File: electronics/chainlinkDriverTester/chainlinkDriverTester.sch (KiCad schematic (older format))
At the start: 144 parts, among them J1 Barrel_Jack_Switch, J10 Sensor C, J11 Sensor D, J12 Motor E, J13 Motor F, J14 Sensor E, J15 Sensor F, J2 Conn_01x03_Female, J22 Power, J26 exp, J27 exp, J28 exp, J29 exp, J3 Motor A, J30 exp, J31 exp, J32 Conn_01x06_Female, J5 Motor B, J6 Motor C, J7 Motor D, J8 Sensor A, J9 Sensor B, SW1 SW_Push, U1 AP7361C-33E, U2 TTGO_TDisplay, U3 VN7007ALH, U4 MCP23017_SS, U5 INA219BxD, U7 Buck

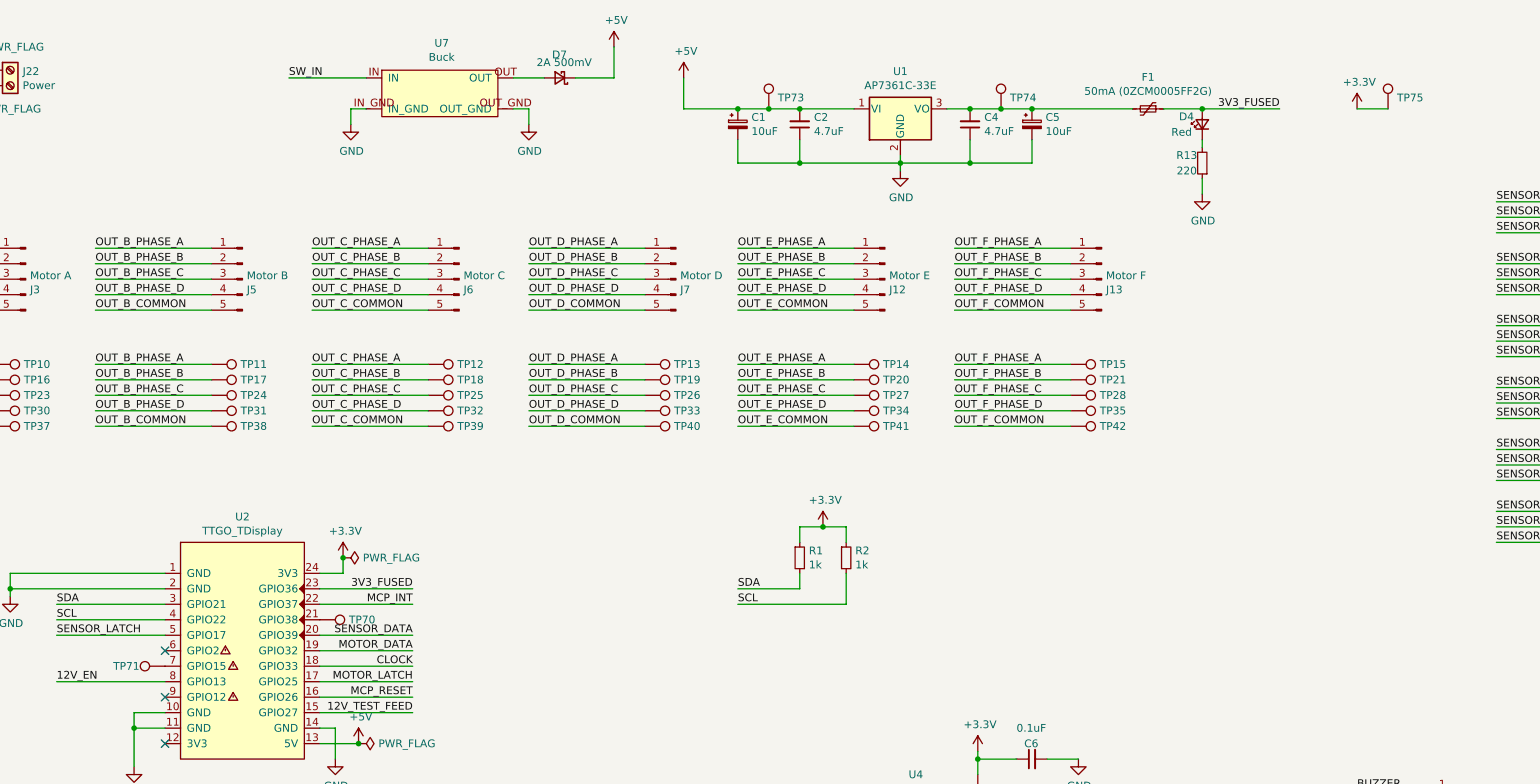
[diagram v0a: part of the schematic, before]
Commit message: Update chainlink driver tester PCB to match schematic with updated T-Display pinout, add extra row of holes for each pin for convenience
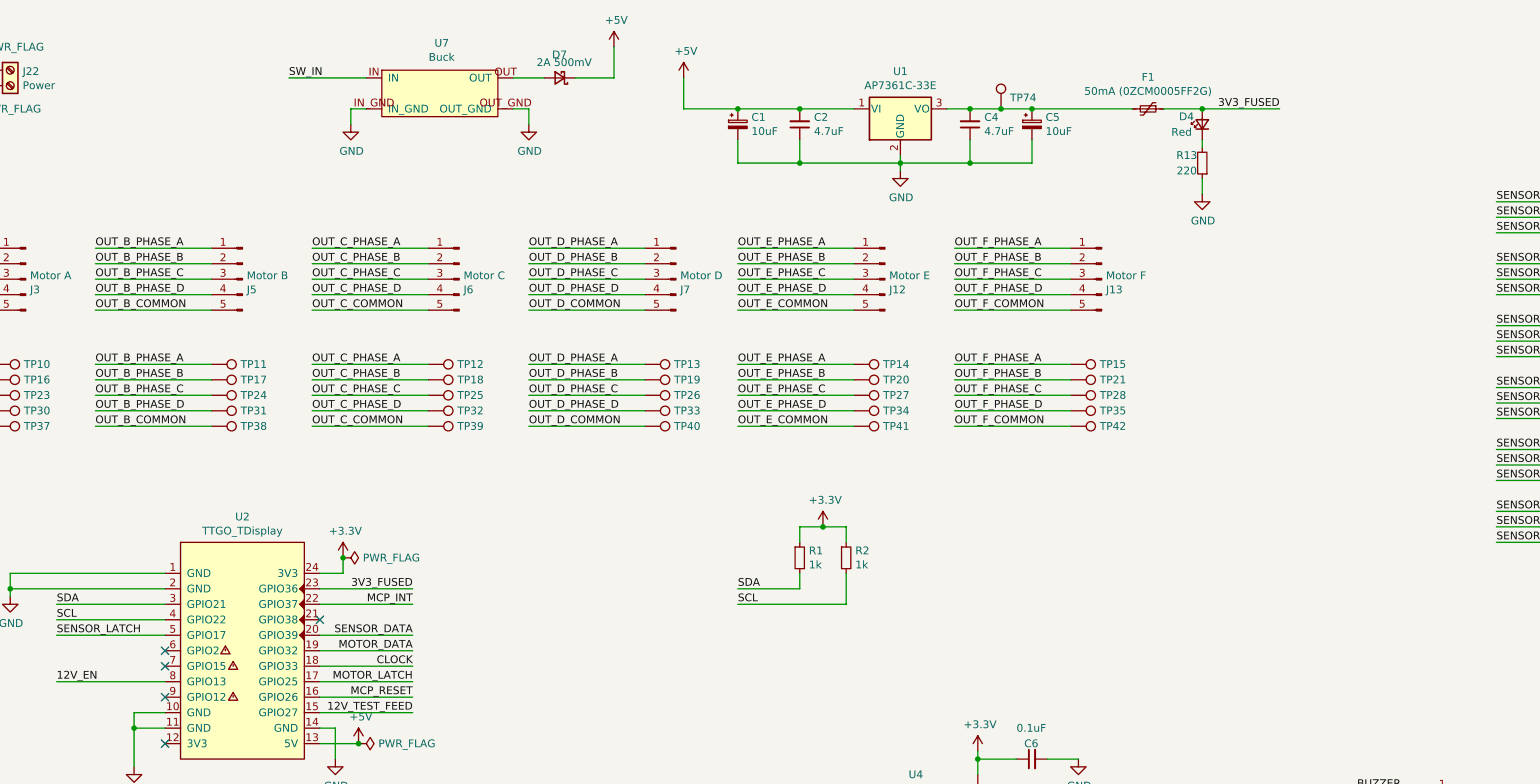
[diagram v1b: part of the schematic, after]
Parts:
- removed TP70, TP71, TP73, TP75: TestPoint, TestPoint:TestPoint_THTPad_D2.0mm_Drill1.0mm, symbol Connector:TestPoint
- U2: footprint ESP32:T-DISPLAY -> ESP32:T-DISPLAY_extra_pins
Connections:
- no-connect marks 20 -> 22
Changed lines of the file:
@@
 F 0 "U2" H 3100 5465 50  0000 C CNN
 F 1 "TTGO_TDisplay" H 3100 5374 50  0000 C CNN
-F 2 "ESP32:T-DISPLAY" H 2900 4650 50  0001 C CNN
+F 2 "ESP32:T-DISPLAY_extra_pins" H 2900 4650 50  0001 C CNN
 F 3 "" H 2900 4650 50  0001 C CNN
 	1    3100 4600
@@
 Connection ~ 6300 1100
 Wire Wire Line
-	6300 1100 6500 1100
-Wire Wire Line
 	6300 1300 6300 1450
 Wire Wire Line
@@
 NoConn ~ 15700 1300
 NoConn ~ 15950 1300
-$Comp
-L Connector:TestPoint TP70
-U 1 1 62B87233
-P 3600 4400
-F 0 "TP70" V 3600 4588 50  0000 L CNN
-F 1 "TestPoint" V 3645 4588 50  0001 L CNN
-F 2 "TestPoint:TestPoint_THTPad_D2.0mm_Drill1.0mm" H 3800 4400 50  0001 C CNN
-F 3 "~" H 3800 4400 50  0001 C CNN
-	1    3600 4400
-	0    1    1    0
-$EndComp
 Wire Wire Line
 	8200 1100 8850 1100
@@
 Wire Wire Line
 	8000 1100 8200 1100
-$Comp
-L Connector:TestPoint TP73
-U 1 1 62BEB5EB
-P 6500 1100
-F 0 "TP73" H 6558 1172 50  0000 L CNN
-F 1 "TestPoint" V 6545 1288 50  0001 L CNN
-F 2 "TestPoint:TestPoint_THTPad_D2.0mm_Drill1.0mm" H 6700 1100 50  0001 C CNN
-F 3 "~" H 6700 1100 50  0001 C CNN
-	1    6500 1100
-	1    0    0    -1
-$EndComp
-Connection ~ 6500 1100
-Wire Wire Line
-	6500 1100 6700 1100
-$Comp
-L Connector:TestPoint TP75
-U 1 1 62BF431E
-P 10500 1100
-F 0 "TP75" H 10558 1172 50  0000 L CNN
-F 1 "TestPoint" V 10545 1288 50  0001 L CNN
-F 2 "TestPoint:TestPoint_THTPad_D2.0mm_Drill1.0mm" H 10700 1100 50  0001 C CNN
-F 3 "~" H 10700 1100 50  0001 C CNN
-	1    10500 1100
-	1    0    0    -1
-$EndComp
-$Comp
-L power:+3.3V #PWR01
-U 1 1 62BFECBC
-P 10300 1100
-F 0 "#PWR01" H 10300 950 50  0001 C CNN
-F 1 "+3.3V" H 10315 1273 50  0000 C CNN
-F 2 "" H 10300 1100 50  0001 C CNN
-F 3 "" H 10300 1100 50  0001 C CNN
-	1    10300 1100
-	1    0    0    -1
-$EndComp
-Wire Wire Line
-	10300 1100 10500 1100
 Text Label 14500 4300 0    50   ~ 0
 SW_IN
@@
 	1    9300 1650
 	1    0    0    -1
-$EndComp
-$Comp
-L Connector:TestPoint TP71
-U 1 1 62B8767D
-P 2600 4700
-F 0 "TP71" V 2600 4950 50  0000 C CNN
-F 1 "TestPoint" V 2704 4772 50  0001 C CNN
-F 2 "TestPoint:TestPoint_THTPad_D2.0mm_Drill1.0mm" H 2800 4700 50  0001 C CNN
-F 3 "~" H 2800 4700 50  0001 C CNN
-	1    2600 4700
-	0    -1   -1   0
 $EndComp
 NoConn ~ 2600 5200
@@
 NoConn ~ 2600 4600
 NoConn ~ 2600 4900
+NoConn ~ 2600 4700
+NoConn ~ 3600 4400
+Wire Wire Line
+	6300 1100 6700 1100
 $EndSCHEMATC

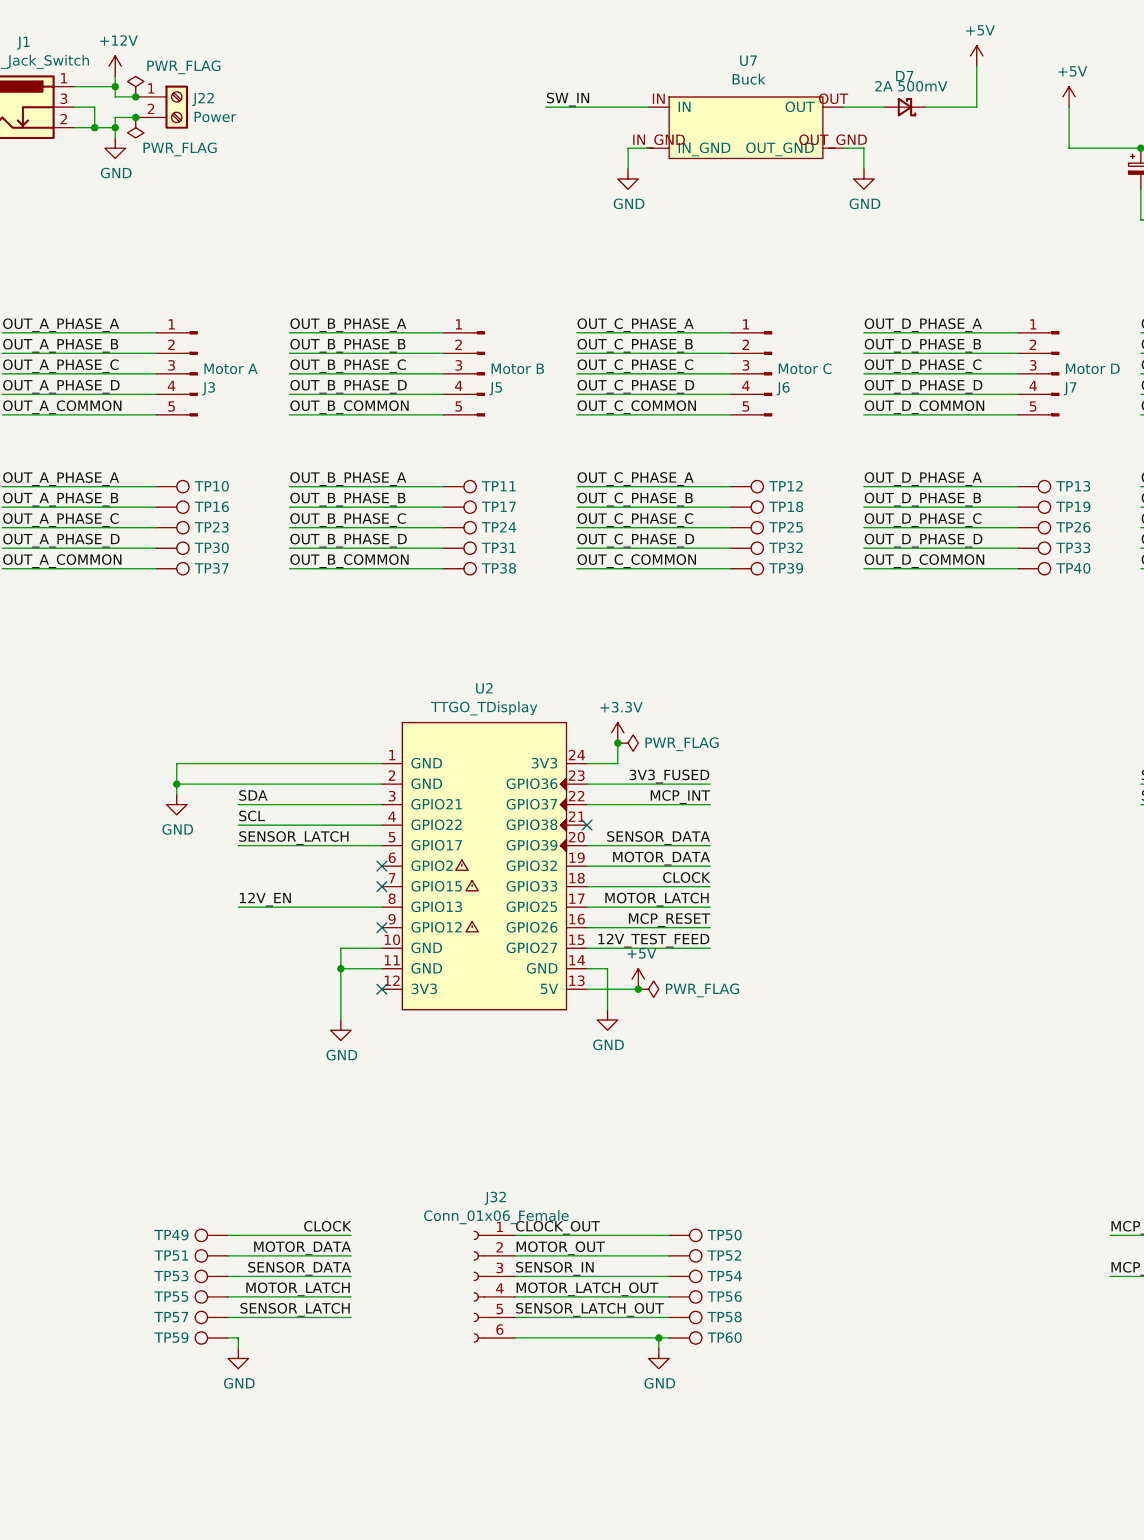
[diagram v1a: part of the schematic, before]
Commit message: Change Chainlink data connections from screw terminals to IDC (#189)
- Replace screw terminals with 2x4 IDC connectors (alternating ground) on Driver, Base, and Tester. Fixes #179
- Change Chainlink Driver Tester to all 1mm pogo pins
- Create new "Buddy" boards for connecting IDC/ribbon cable to T-Display or a breadboard
- Big readme cleanup and reorganization for clarity (hopefully!)
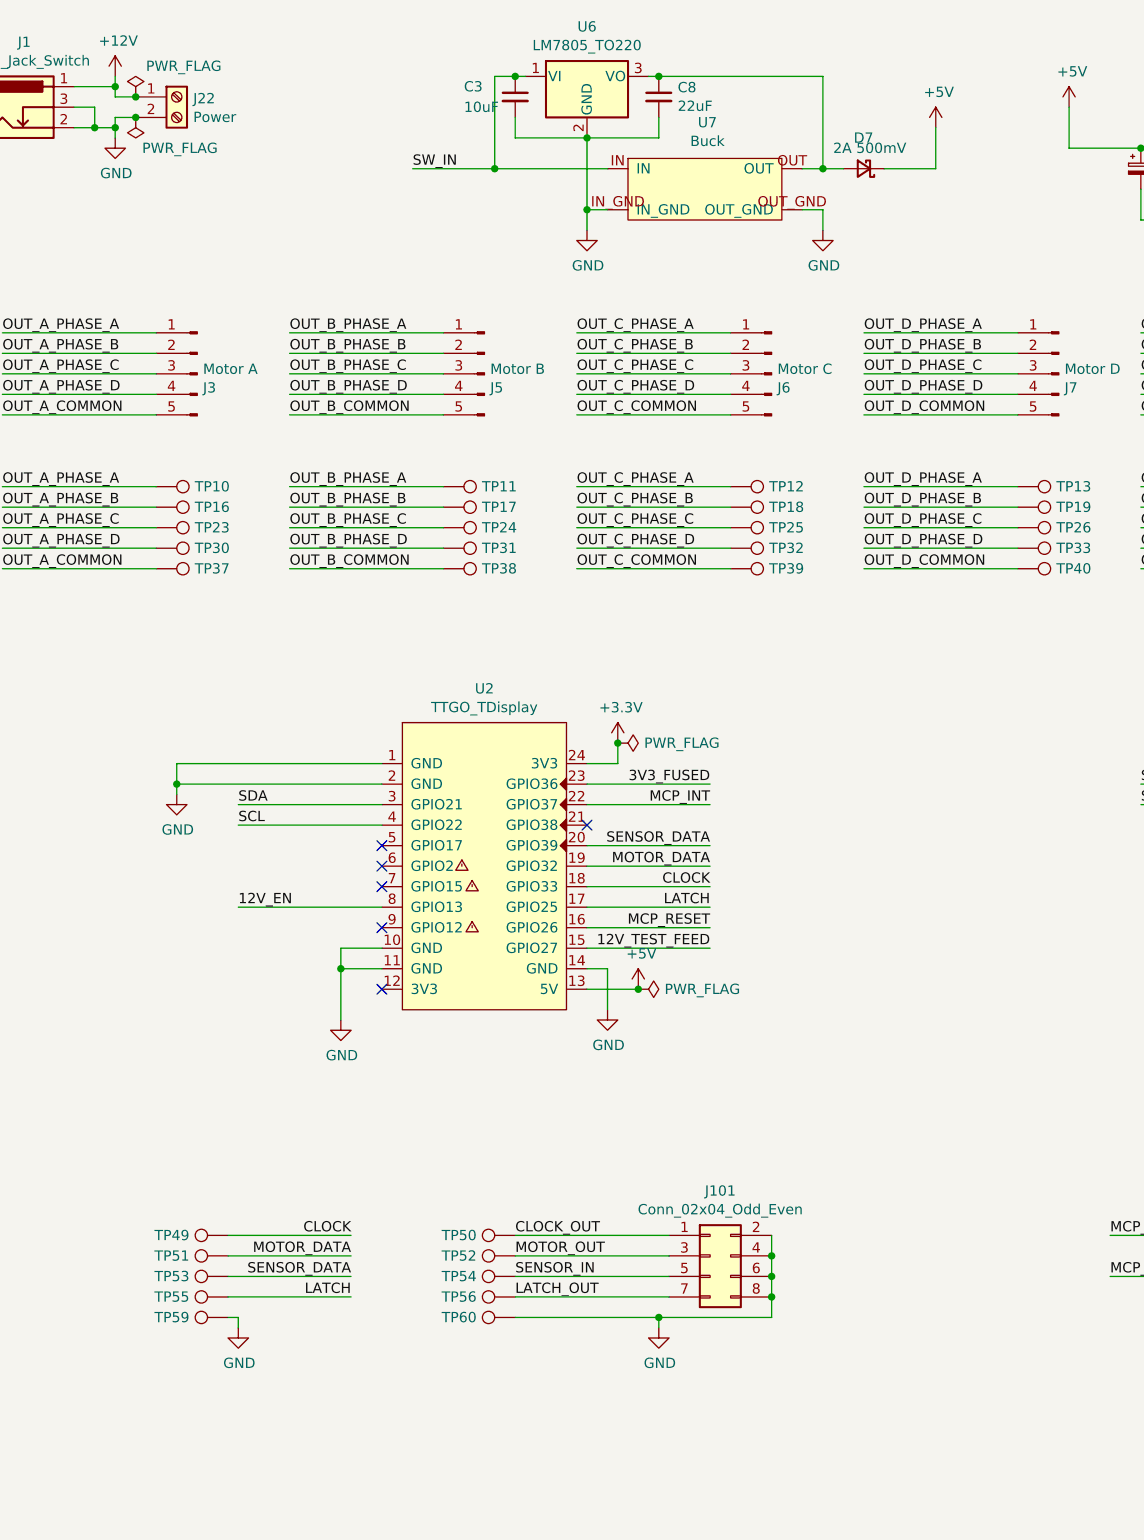
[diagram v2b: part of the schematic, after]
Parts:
- removed J32: Conn_01x06_Female, Connector_PinSocket_2.54mm:PinSocket_1x06_P2.54mm_Vertical, symbol Connector:Conn_01x06_Female
- removed TP57, TP58: TestPoint, pogoPins:pogo2mm, symbol Connector:TestPoint
- added C3: 10uF, Capacitor_SMD:C_1206_3216Metric, symbol Device:C_Small
- added C8: 22uF, Capacitor_SMD:C_1206_3216Metric, symbol Device:C_Small
- added J101: Conn_02x04_Odd_Even, ModifiedSymbols:IDC-Header_2x04_P2.54mm_Vertical, symbol Connector_Generic:Conn_02x04_Odd_Even
- added U6: LM7805_TO220, Package_TO_SOT_THT:TO-220-3_Vertical, symbol Regulator_Linear:LM7805_TO220
- TP49, TP50, TP51, TP52, TP53, TP54, TP55, TP56, TP59, TP60, TP63, TP64, TP65, TP66, TP67, TP68: footprint pogoPins:pogo2mm -> pogoPins:pogo1mm
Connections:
- net CLOCK_OUT: now also J101.1 (Pin_1)
- net GND: now also C3.2, C8.2, J101.2 (Pin_2), J101.4 (Pin_4), J101.6 (Pin_6), J101.8 (Pin_8), U6.2 (GND)
- net MOTOR_OUT: now also J101.3 (Pin_3)
- net SENSOR_IN: now also J101.5 (Pin_5)
- net SW_IN: now also C3.1, U6.1 (VI)
- net at D7.2 (A), U7.OUT: now also C8.1, U6.3 (VO)
- net MOTOR_LATCH renamed LATCH
- net MOTOR_LATCH_OUT renamed LATCH_OUT
- net LATCH_OUT: now also J101.7 (Pin_7)
- net SENSOR_LATCH: no longer names the net of U2.5 (GPIO17)
- no-connect marks 22 -> 23
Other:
- moved on the sheet: D7, TP50, TP52, TP54, TP56, TP59, TP60, U7
